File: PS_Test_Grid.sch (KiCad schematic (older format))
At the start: 50 parts, among them J1 CONN_01X03, J10 CONN_01X01, J2 CONN_01X01, J3 CONN_01X01, J4 CONN_01X01, J5 CONN_01X01, J6 CONN_01X03, J7 CONN_01X01, J8 CONN_01X01, J9 CONN_01X01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

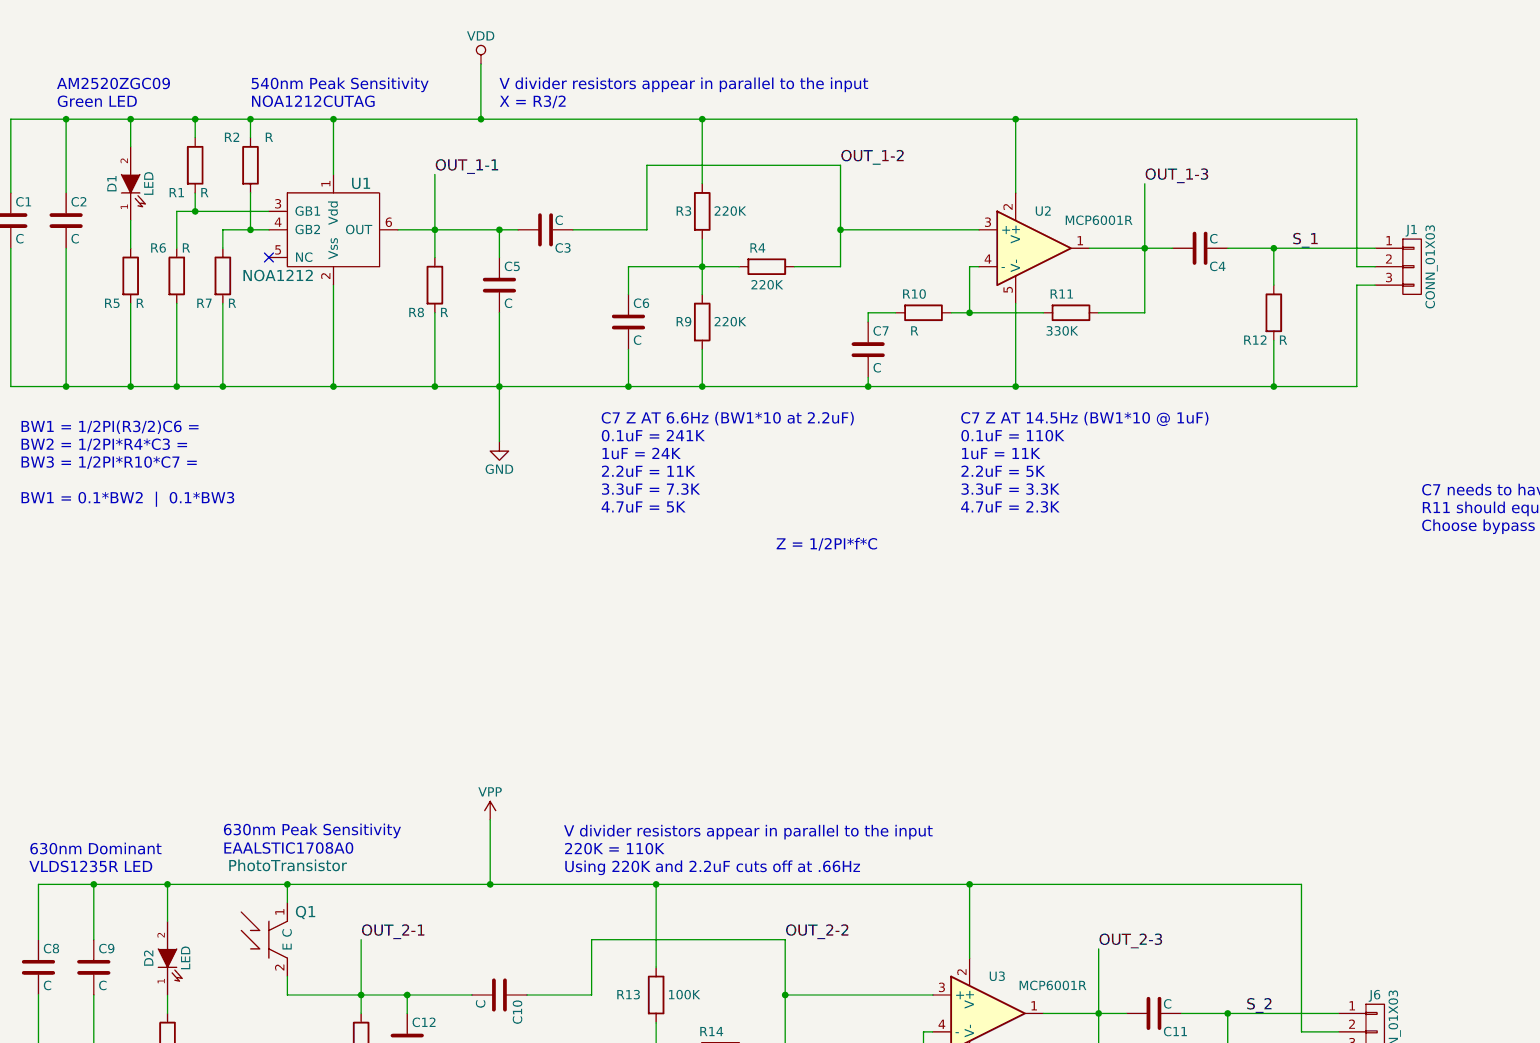
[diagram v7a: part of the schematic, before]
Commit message: Layout Circuit Add Protection Diode to Schem
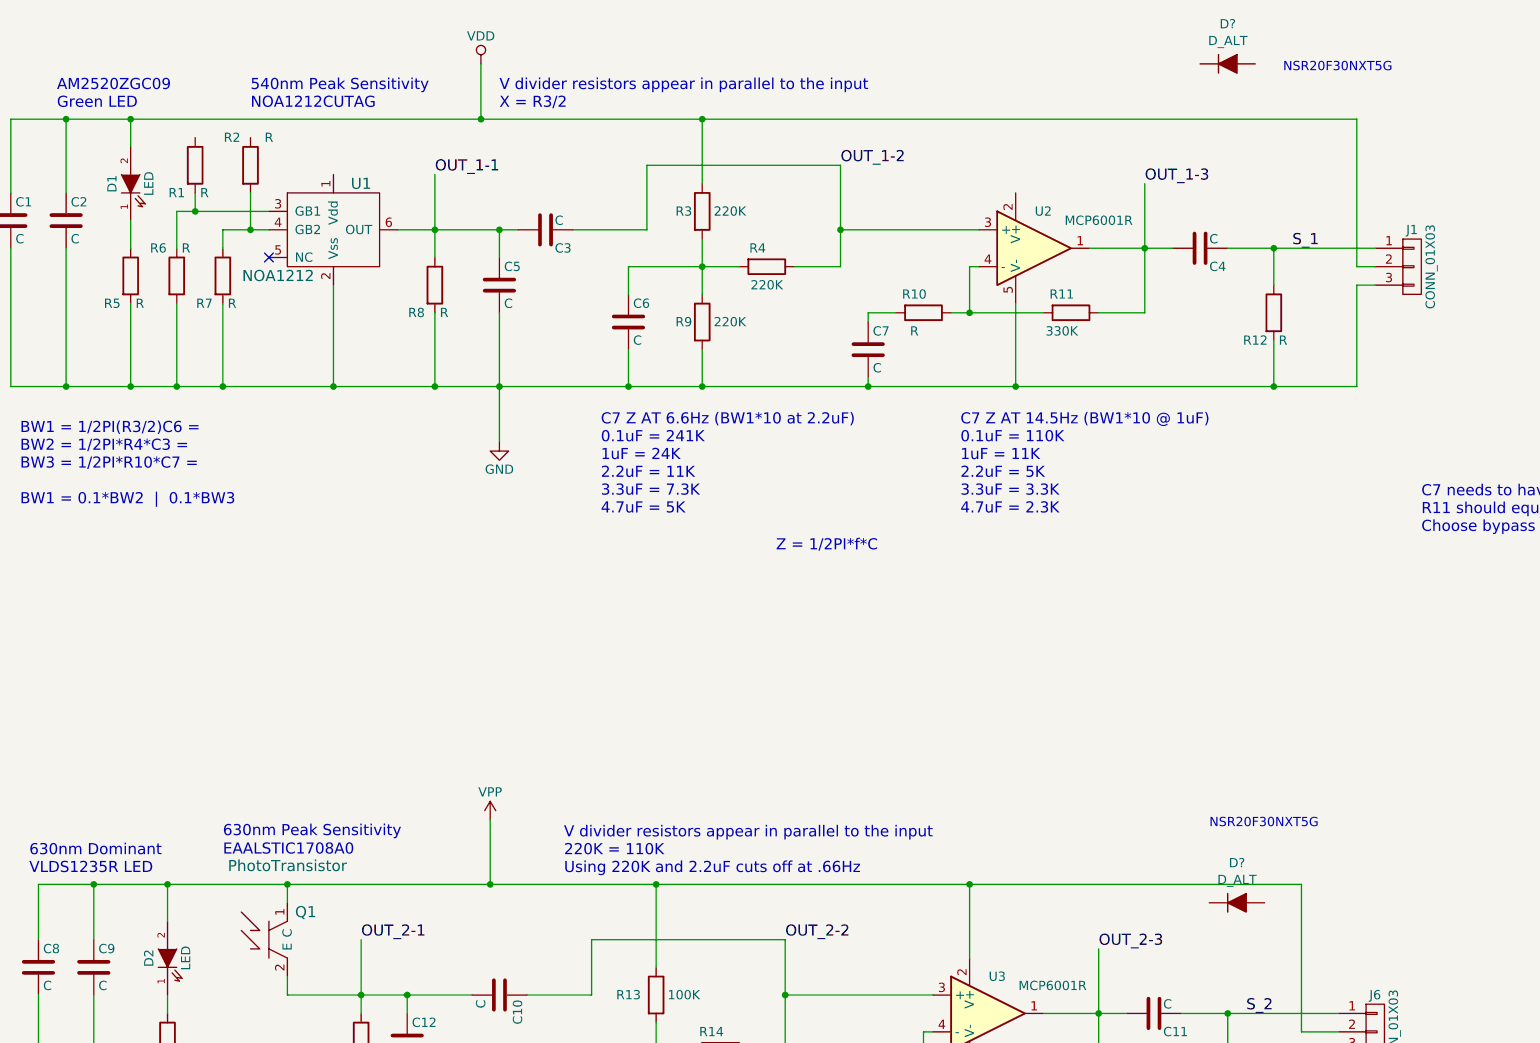
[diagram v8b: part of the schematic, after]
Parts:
- added D? (x2): D_ALT, symbol Device:D_ALT
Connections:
- net VDD: no longer R1.1, R2.1, U1.1 (Vdd), U2.2 (V+)
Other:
- note added: "NSR20F30NXT5G"
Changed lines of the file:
@@
 Connection ~ 8050 3550
 Wire Wire Line
-	7150 2100 7150 2400
-Wire Wire Line
 	5400 2100 5700 2100
 Wire Wire Line
 	7950 2100 7950 1800
-Wire Wire Line
-	10850 2100 10850 2500
 Connection ~ 7950 2100
 Wire Wire Line
 	6050 2250 6050 2100
-Connection ~ 7150 2100
 Wire Wire Line
 	6050 2800 6050 2650
@@
 Connection ~ 10600 3150
 Wire Wire Line
-	6700 2200 6700 2100
-Connection ~ 6700 2100
-Wire Wire Line
-	6400 2200 6400 2100
-Connection ~ 6400 2100
-Wire Wire Line
 	6300 3550 6300 3100
 Connection ~ 6300 3550
@@
 Wire Wire Line
 	6900 6250 6900 6350
-Connection ~ 8000 6250
-Wire Wire Line
-	6250 6250 6250 6450
-Connection ~ 6900 6250
 Wire Wire Line
 	6250 6850 6250 6950
@@
 Wire Wire Line
 	5700 2500 5700 2100
-Connection ~ 6050 2100
 Wire Wire Line
 	5700 2800 5700 3550
@@
 Wire Wire Line
 	5400 2500 5400 2100
-Connection ~ 5700 2100
 Wire Wire Line
 	5400 2800 5400 3550
@@
 	10600 7700 10600 7250
 Wire Wire Line
-	10600 6250 10600 6650
-Wire Wire Line
 	8900 6250 8900 6700
 Connection ~ 8900 6250
@@
 $EndComp
 Connection ~ 8550 7700
-Connection ~ 5850 6250
-Connection ~ 6250 6250
 Connection ~ 6250 7700
 Wire Wire Line
@@
 Wire Wire Line
 	12700 2900 12700 2100
-Connection ~ 10850 2100
 Connection ~ 12250 2800
 Connection ~ 12250 3550
-Connection ~ 10600 6250
 Connection ~ 12000 7700
 Connection ~ 12000 6950
@@
 	7950 2100 9150 2100
 Wire Wire Line
-	7150 2100 7950 2100
-Wire Wire Line
 	7150 3550 7700 3550
 Wire Wire Line
@@
 	8050 2700 8150 2700
 Wire Wire Line
-	9150 2100 10850 2100
-Wire Wire Line
 	9150 3550 10050 3550
 Wire Wire Line
@@
 	10600 3150 11000 3150
 Wire Wire Line
-	6700 2100 7150 2100
-Wire Wire Line
-	6400 2100 6700 2100
-Wire Wire Line
 	6300 3550 6550 3550
 Wire Wire Line
@@
 	8000 6250 8900 6250
 Wire Wire Line
+	7300 7700 7550 7700
+Wire Wire Line
+	10050 3550 10850 3550
+Wire Wire Line
+	6050 3550 6300 3550
+Wire Wire Line
+	5700 3550 6050 3550
+Wire Wire Line
+	11550 2800 11700 2800
+Wire Wire Line
+	11550 2800 11550 3150
+Wire Wire Line
+	10850 3550 12250 3550
+Wire Wire Line
+	8900 7700 9800 7700
+Wire Wire Line
+	8900 7150 8900 7250
+Wire Wire Line
+	8900 7150 9100 7150
+Wire Wire Line
+	10350 7300 10750 7300
+Wire Wire Line
+	9800 7700 10600 7700
+Wire Wire Line
+	11300 6950 11450 6950
+Wire Wire Line
+	11300 6950 11300 7300
+Wire Wire Line
+	8550 7700 8900 7700
+Wire Wire Line
+	6250 7700 7300 7700
+Wire Wire Line
+	5850 7700 6250 7700
+Wire Wire Line
+	10600 7700 12000 7700
+Wire Wire Line
+	8750 3550 9150 3550
+Wire Wire Line
+	9900 2700 9900 2900
+Wire Wire Line
+	9600 6850 9600 7150
+Wire Wire Line
+	12250 2800 12800 2800
+Wire Wire Line
+	12250 3550 12700 3550
+Wire Wire Line
+	12000 7700 12400 7700
+Wire Wire Line
+	12000 6950 12600 6950
+$Comp
+L Device:D_ALT D?
+U 1 1 5BFF69DD
+P 12000 1800
+F 0 "D?" H 12000 2016 50  0000 C CNN
+F 1 "D_ALT" H 12000 1925 50  0000 C CNN
+F 2 "" H 12000 1800 50  0001 C CNN
+F 3 "~" H 12000 1800 50  0001 C CNN
+	1    12000 1800
+	1    0    0    -1
+$EndComp
+$Comp
+L Device:D_ALT D?
+U 1 1 5BFF6A6F
+P 12050 6350
+F 0 "D?" H 12050 6566 50  0000 C CNN
+F 1 "D_ALT" H 12050 6475 50  0000 C CNN
+F 2 "" H 12050 6350 50  0001 C CNN
+F 3 "~" H 12050 6350 50  0001 C CNN
+	1    12050 6350
+	1    0    0    -1
+$EndComp
+Wire Wire Line
+	9150 2100 12700 2100
+Wire Wire Line
+	6050 2100 7950 2100
+Wire Wire Line
+	6250 6250 6250 6450
+Wire Wire Line
+	10600 6250 12400 6250
+Wire Wire Line
+	8900 6250 10600 6250
+Connection ~ 10600 6250
+Wire Wire Line
+	10600 6250 10600 6650
+Connection ~ 5850 6250
+Wire Wire Line
+	5850 6250 6250 6250
+Connection ~ 8000 6250
+Wire Wire Line
 	6900 6250 8000 6250
-Wire Wire Line
-	7300 7700 7550 7700
-Wire Wire Line
-	10050 3550 10850 3550
-Wire Wire Line
-	6050 2100 6400 2100
-Wire Wire Line
-	6050 3550 6300 3550
+Connection ~ 6900 6250
+Connection ~ 6250 6250
+Wire Wire Line
+	6250 6250 6900 6250
+Connection ~ 6050 2100
+Connection ~ 5700 2100
 Wire Wire Line
 	5700 2100 6050 2100
-Wire Wire Line
-	5700 3550 6050 3550
-Wire Wire Line
-	11550 2800 11700 2800
-Wire Wire Line
-	11550 2800 11550 3150
-Wire Wire Line
-	10850 3550 12250 3550
-Wire Wire Line
-	8900 6250 10600 6250
-Wire Wire Line
-	8900 7700 9800 7700
-Wire Wire Line
-	8900 7150 8900 7250
-Wire Wire Line
-	8900 7150 9100 7150
-Wire Wire Line
-	10350 7300 10750 7300
-Wire Wire Line
-	9800 7700 10600 7700
-Wire Wire Line
-	11300 6950 11450 6950
-Wire Wire Line
-	11300 6950 11300 7300
-Wire Wire Line
-	8550 7700 8900 7700
-Wire Wire Line
-	5850 6250 6250 6250
-Wire Wire Line
-	6250 6250 6900 6250
-Wire Wire Line
-	6250 7700 7300 7700
-Wire Wire Line
-	5850 7700 6250 7700
-Wire Wire Line
-	10600 7700 12000 7700
-Wire Wire Line
-	8750 3550 9150 3550
-Wire Wire Line
-	9900 2700 9900 2900
-Wire Wire Line
-	9600 6850 9600 7150
-Wire Wire Line
-	10850 2100 12700 2100
-Wire Wire Line
-	12250 2800 12800 2800
-Wire Wire Line
-	12250 3550 12700 3550
-Wire Wire Line
-	10600 6250 12400 6250
-Wire Wire Line
-	12000 7700 12400 7700
-Wire Wire Line
-	12000 6950 12600 6950
+Text Notes 11900 5950 0    50   ~ 0
+NSR20F30NXT5G
+Text Notes 12300 1850 0    50   ~ 0
+NSR20F30NXT5G
 $EndSCHEMATC
